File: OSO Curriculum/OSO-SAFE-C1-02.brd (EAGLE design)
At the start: 50.8 x 22.9 mm, 19 parts, among them U1 LM1117T-3.3, U2 ATSAMD11D14A-SSNT

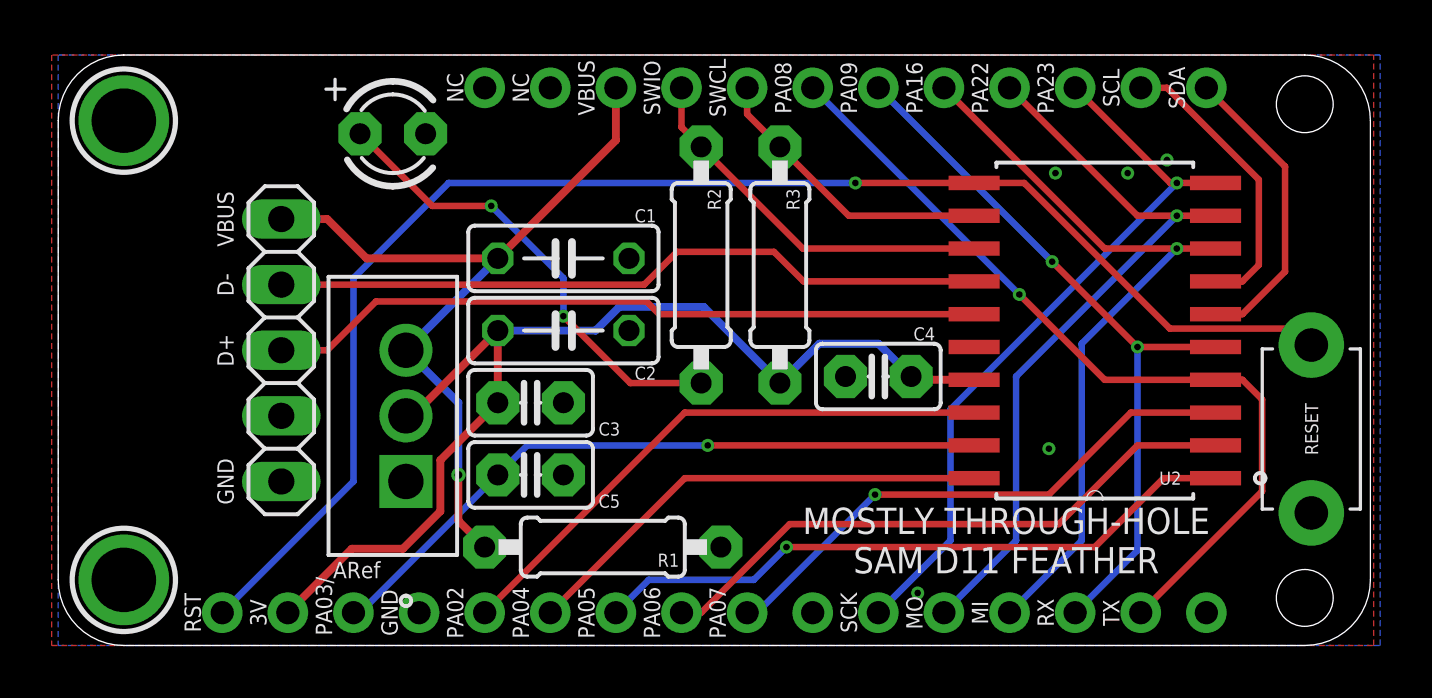
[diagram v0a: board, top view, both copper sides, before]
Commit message: scoot usb breakout up a bit
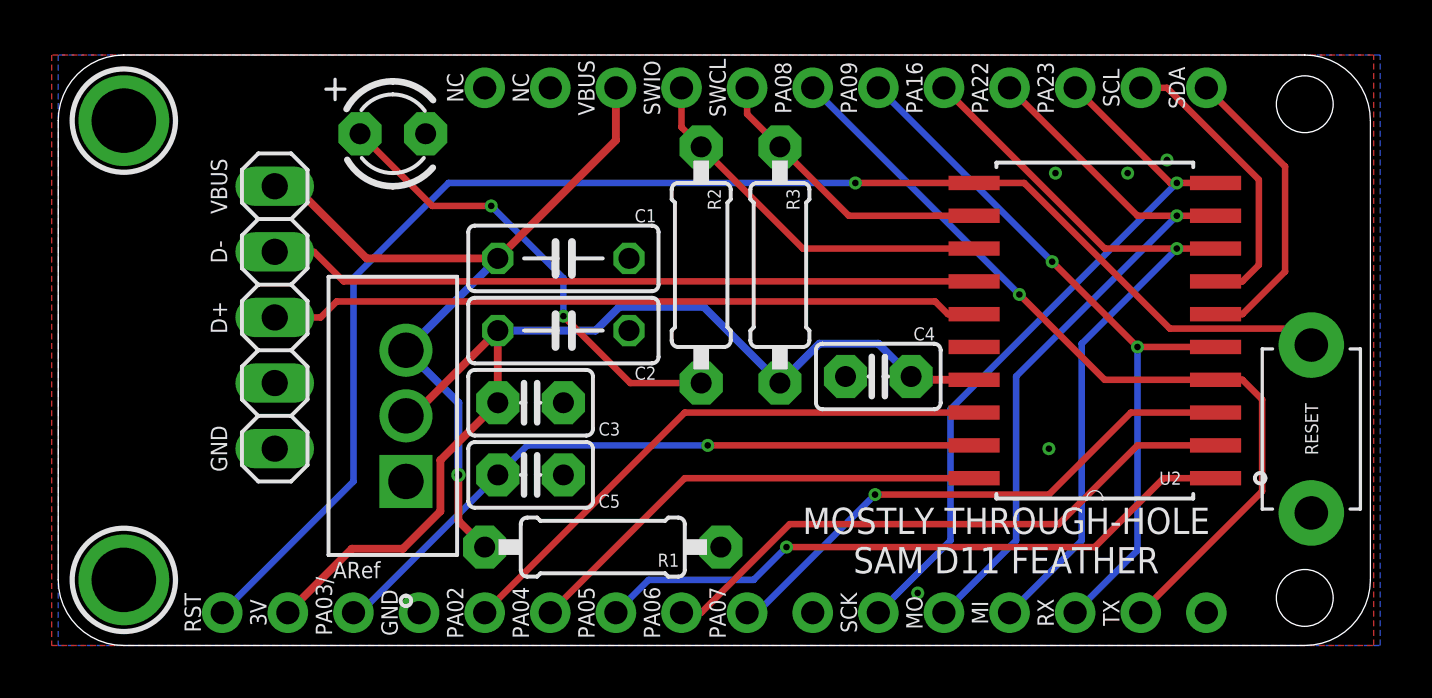
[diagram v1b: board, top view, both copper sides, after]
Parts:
- moved USB 1.30 mm to (8.38, 12.7)
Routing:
- net VBUS: track 31.4 -> 32.2 mm
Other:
- board text added: "OSO-SAFE-C1-02"
- board text removed: "OSO-SAFE-C1-01"
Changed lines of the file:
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@@
 the Book
 #4</text>
-<text x="9.906" y="21.59" size="0.8128" layer="22" font="vector" ratio="18" rot="MR180" align="center">OSO-SAFE-C1-01</text>
-<rectangle x1="0.254" y1="1.27" x2="10.414" y2="21.59" layer="43"/>
+<text x="9.906" y="21.59" size="0.8128" layer="22" font="vector" ratio="18" rot="MR180" align="center">OSO-SAFE-C1-02</text>
+<rectangle x1="0" y1="2.54" x2="10.16" y2="22.86" layer="43"/>
 <text x="25.527" y="21.59" size="0.635" layer="21" font="vector" ratio="12" rot="R90" align="center">SWCL</text>
 <text x="25.527" y="1.27" size="0.635" layer="21" font="vector" ratio="12" rot="R90" align="center">PA07</text>
-<text x="6.477" y="16.51" size="0.635" layer="21" font="vector" ratio="18" rot="R270" align="center">VBUS</text>
-<text x="6.477" y="13.97" size="0.635" layer="21" font="vector" ratio="18" rot="R270" align="center">D-</text>
-<text x="6.477" y="11.43" size="0.635" layer="21" font="vector" ratio="18" rot="R270" align="center">D+</text>
-<text x="6.477" y="6.35" size="0.635" layer="21" font="vector" ratio="18" rot="R270" align="center">GND</text>
-<text x="10.795" y="16.51" size="0.635" layer="22" font="vector" ratio="18" rot="SMR270" align="center">VBUS</text>
-<text x="10.795" y="13.97" size="0.635" layer="22" font="vector" ratio="18" rot="SMR270" align="center">D-</text>
-<text x="10.795" y="11.43" size="0.635" layer="22" font="vector" ratio="18" rot="SMR270" align="center">D+</text>
-<text x="10.795" y="6.35" size="0.635" layer="22" font="vector" ratio="18" rot="SMR270" align="center">GND</text>
+<text x="6.223" y="17.78" size="0.635" layer="21" font="vector" ratio="18" rot="R270" align="center">VBUS</text>
+<text x="6.223" y="15.24" size="0.635" layer="21" font="vector" ratio="18" rot="R270" align="center">D-</text>
+<text x="6.223" y="12.7" size="0.635" layer="21" font="vector" ratio="18" rot="R270" align="center">D+</text>
+<text x="6.223" y="7.62" size="0.635" layer="21" font="vector" ratio="18" rot="R270" align="center">GND</text>
+<text x="10.541" y="17.78" size="0.635" layer="22" font="vector" ratio="18" rot="SMR270" align="center">VBUS</text>
+<text x="10.541" y="15.24" size="0.635" layer="22" font="vector" ratio="18" rot="SMR270" align="center">D-</text>
+<text x="10.541" y="12.7" size="0.635" layer="22" font="vector" ratio="18" rot="SMR270" align="center">D+</text>
+<text x="10.541" y="7.62" size="0.635" layer="22" font="vector" ratio="18" rot="SMR270" align="center">GND</text>
 <text x="26.416" y="20.574" size="0.6096" layer="22" font="vector" ratio="12" rot="SMR270" align="center-left">PA30/SWCLK</text>
 <text x="29.21" y="20.574" size="0.6096" layer="22" font="vector" ratio="12" rot="SMR270" align="center-left">PA08</text>
@@
 <wire x1="37.465" y1="10.541" x2="39.116" y2="8.89" width="0.254" layer="22"/>
 <wire x1="39.116" y1="8.89" x2="39.116" y2="4.445" width="0.254" layer="22"/>
-<wire x1="39.497" y1="7.493" x2="41.656" y2="5.334" width="0.254" layer="22"/>
+<wire x1="39.624" y1="7.366" x2="41.656" y2="5.334" width="0.254" layer="22"/>
 <wire x1="41.656" y1="5.334" x2="41.656" y2="4.445" width="0.254" layer="22"/>
 <text x="16.51" y="20.574" size="0.6096" layer="22" font="vector" ratio="12" rot="SMR270" align="center-left">VBAT
@@
 <attribute name="VENDOR" value="Texas Instruments" x="12.446" y="11.43" size="1.778" layer="27" rot="R90" display="off"/>
 </element>
-<element name="USB" library="pinhead" library_urn="urn:adsk.eagle:library:325" package="1X05" package3d_urn="urn:adsk.eagle:package:22469/2" value="" x="8.636" y="11.43" smashed="yes" rot="R270">
-<attribute name="VALUE" x="5.461" y="17.78" size="1.27" layer="27" rot="R270"/>
+<element name="USB" library="pinhead" library_urn="urn:adsk.eagle:library:325" package="1X05" package3d_urn="urn:adsk.eagle:package:22469/2" value="" x="8.382" y="12.7" smashed="yes" rot="R270">
+<attribute name="VALUE" x="5.207" y="19.05" size="1.27" layer="27" rot="R270"/>
 </element>
 <element name="R2" library="adafruit" package="0207/9" value="1K" x="24.892" y="14.732" smashed="yes" rot="R270">
@@
 <contactref element="R1" pad="2"/>
 <wire x1="13.462" y1="11.43" x2="17.018" y2="14.986" width="0.3048" layer="16"/>
-<wire x1="11.938" y1="14.986" x2="10.414" y2="16.51" width="0.3048" layer="1"/>
-<wire x1="10.414" y1="16.51" x2="8.636" y2="16.51" width="0.3048" layer="1"/>
+<wire x1="11.938" y1="14.986" x2="9.144" y2="17.78" width="0.3048" layer="1"/>
+<wire x1="9.144" y1="17.78" x2="8.382" y2="17.78" width="0.3048" layer="1"/>
 <wire x1="11.938" y1="14.986" x2="17.018" y2="14.986" width="0.3048" layer="1"/>
 <wire x1="21.59" y1="21.59" x2="21.59" y2="19.558" width="0.3048" layer="1"/>
@@
 <signal name="USB_P">
 <contactref element="U2" pad="15"/>
-<wire x1="35.4584" y1="12.827" x2="23.2664" y2="12.827" width="0.254" layer="1"/>
-<wire x1="23.2664" y1="12.827" x2="22.7748375" y2="13.3185625" width="0.254" layer="1"/>
-<wire x1="10.414" y1="11.43" x2="12.3025625" y2="13.3185625" width="0.254" layer="1"/>
-<wire x1="12.3025625" y1="13.3185625" x2="22.7748375" y2="13.3185625" width="0.254" layer="1"/>
+<wire x1="35.4584" y1="12.827" x2="34.4424" y2="12.827" width="0.254" layer="1"/>
+<wire x1="34.4424" y1="12.827" x2="33.9508375" y2="13.3185625" width="0.254" layer="1"/>
+<wire x1="10.16" y1="12.7" x2="10.7785625" y2="13.3185625" width="0.254" layer="1"/>
+<wire x1="10.7785625" y1="13.3185625" x2="33.9508375" y2="13.3185625" width="0.254" layer="1"/>
 <contactref element="USB" pad="3"/>
-<wire x1="8.636" y1="11.43" x2="10.414" y2="11.43" width="0.254" layer="1"/>
+<wire x1="8.382" y1="12.7" x2="10.16" y2="12.7" width="0.254" layer="1"/>
 </signal>
 <signal name="USB_N">
 <contactref element="U2" pad="14"/>
-<wire x1="28.8544" y1="14.097" x2="35.4584" y2="14.097" width="0.254" layer="1"/>
-<wire x1="27.7114" y1="15.24" x2="28.8544" y2="14.097" width="0.254" layer="1"/>
-<wire x1="23.955384375" y1="15.24" x2="27.7114" y2="15.24" width="0.254" layer="1"/>
-<wire x1="22.685384375" y1="13.97" x2="23.955384375" y2="15.24" width="0.254" layer="1"/>
 <contactref element="USB" pad="2"/>
-<wire x1="8.636" y1="13.97" x2="22.685384375" y2="13.97" width="0.254" layer="1"/>
+<wire x1="11.049" y1="14.097" x2="9.906" y2="15.24" width="0.254" layer="1"/>
+<wire x1="8.382" y1="15.24" x2="9.906" y2="15.24" width="0.254" layer="1"/>
+<wire x1="35.4584" y1="14.097" x2="11.049" y2="14.097" width="0.254" layer="1"/>
 </signal>
 <signal name="PA05">
